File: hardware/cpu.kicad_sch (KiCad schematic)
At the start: 62 parts, among them Q5 MMBT3904, U1 H3, Y1 32kHz, Y3 24MHz

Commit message: Even more routing
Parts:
- removed C9: 100nF, Capacitor_SMD:C_0402_1005Metric, symbol Device:C
- added C41: 100nF, Capacitor_SMD:C_0402_1005Metric, symbol Device:C
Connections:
- net GND: now also C41.2
- net PWR_LED: now also U1.V2 (PL10)
- net VREF: now also C41.1
- net WL_REG_ON: now also U1.B1 (PG13); no longer U1.F13 (PA8)
- no-connect marks 29 -> 28
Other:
- moved on the sheet: C129, C130, C3, C4, Q5, R63, R64, R65

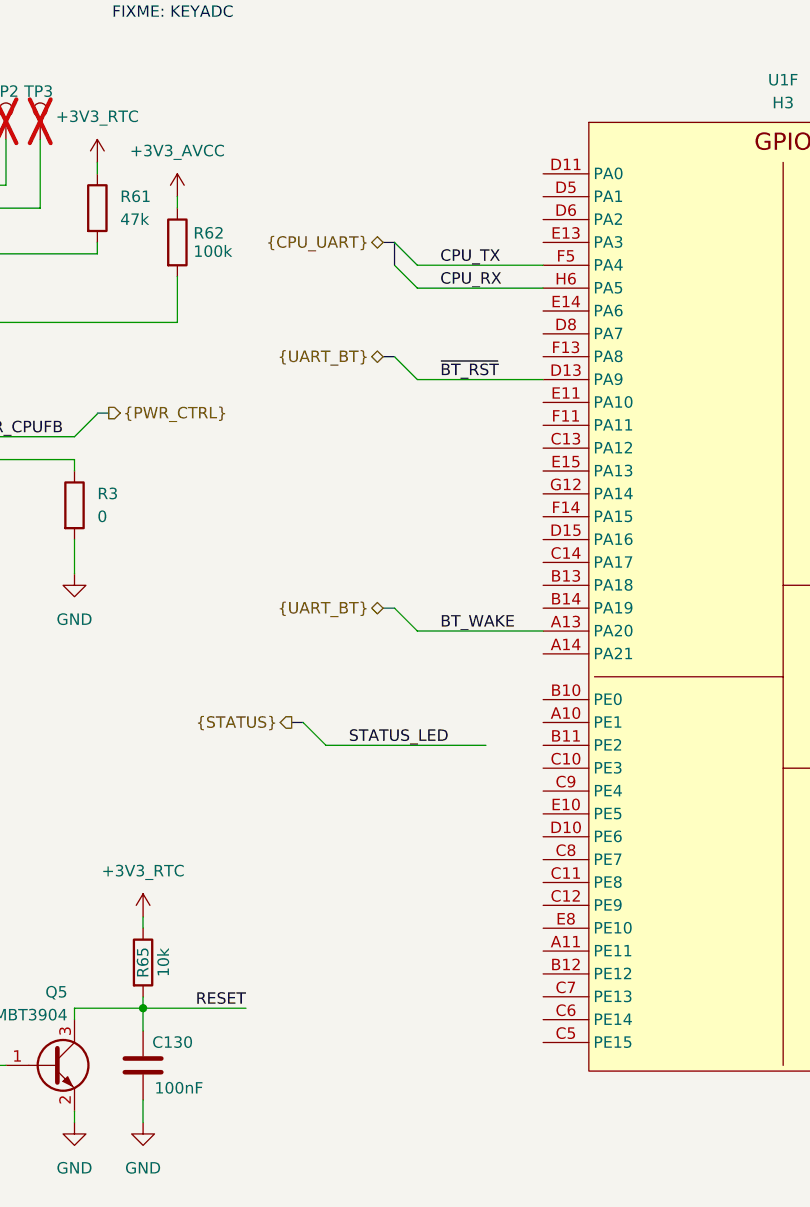
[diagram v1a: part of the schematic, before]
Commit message: Less than 100 traces left
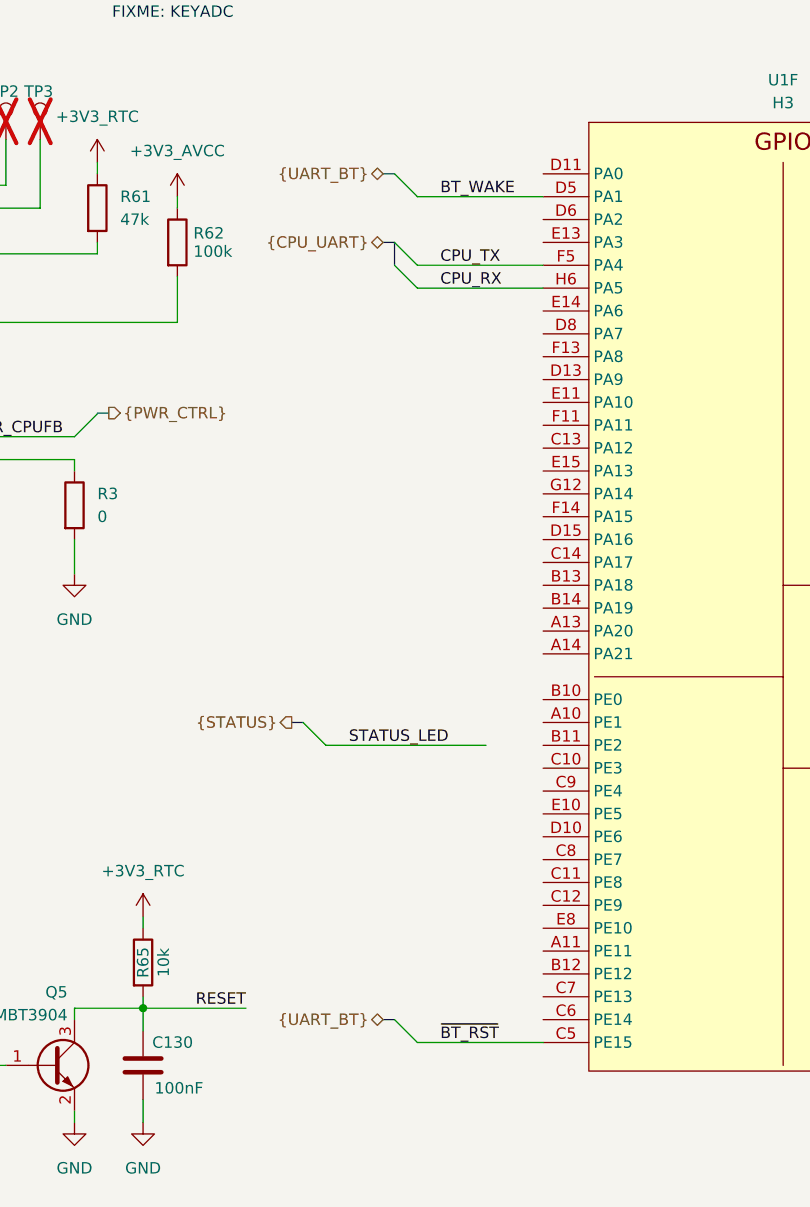
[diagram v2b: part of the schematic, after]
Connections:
- net BT_WAKE: now also U1.D5 (PA1); no longer U1.A13 (PA20)
- net ~{BT_RST}: now also U1.C5 (PE15); no longer U1.D13 (PA9)
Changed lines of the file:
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@@
 	)
 	(bus_entry
-		(at 302.26 154.94)
+		(at 302.26 228.6)
 		(size -2.54 -2.54)
 		(stroke
@@
 	)
 	(bus_entry
-		(at 302.26 182.88)
+		(at 302.26 134.62)
 		(size -2.54 -2.54)
 		(stroke
@@
 	(wire
 		(pts
-			(xy 302.26 182.88) (xy 316.23 182.88)
+			(xy 302.26 134.62) (xy 316.23 134.62)
 		)
 		(stroke
@@
 	(wire
 		(pts
-			(xy 302.26 154.94) (xy 316.23 154.94)
+			(xy 302.26 228.6) (xy 316.23 228.6)
 		)
 		(stroke
@@
 	(bus
 		(pts
-			(xy 299.72 152.4) (xy 298.45 152.4)
+			(xy 299.72 226.06) (xy 298.45 226.06)
 		)
 		(stroke
@@
 	(bus
 		(pts
-			(xy 299.72 180.34) (xy 298.45 180.34)
+			(xy 299.72 132.08) (xy 298.45 132.08)
 		)
 		(stroke
@@
 	)
 	(label "BT_WAKE"
-		(at 304.8 182.88 0)
+		(at 304.8 134.62 0)
 		(effects
 			(font
@@
 	)
 	(label "~{BT_RST}"
-		(at 304.8 154.94 0)
+		(at 304.8 228.6 0)
 		(effects
 			(font
@@
 	(hierarchical_label "{UART_BT}"
 		(shape bidirectional)
-		(at 298.45 152.4 180)
+		(at 298.45 226.06 180)
 		(effects
 			(font
@@
 	(hierarchical_label "{UART_BT}"
 		(shape bidirectional)
-		(at 298.45 180.34 180)
+		(at 298.45 132.08 180)
 		(effects
 			(font
